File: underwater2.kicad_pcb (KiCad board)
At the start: 2 copper layers, 99.6 x 99.1 mm, 125 parts, among them IC1 KST10MTF, IC2 KST10MTF, IC3 ACT4070BYH-T, IC4 ICM-20948, IC5 MAX662ACSA+, IC6 MCP73842T-840I_UN, J1 Conn_01x10_Female, J10 momentary switch, J11 external regurator, J12 ICM20948 out, J13 Motor1, J14 MotorPow, J15 Motor2, J16 Conn_01x02_Female, J17 Conn_01x02_Female, J18 Conn_01x02_Female, J2 USB_C_Receptacle_USB2.0, J3 Raspberry_Pi_2_3, J4 serial, J5 Water, J6 serial2, J7 5v pow, J8 5v pow, J9 Power, Q1 2SC2712-Y,LF, Q2 2SC2712-Y,LF, Q3 2SC2712-Y,LF, Q4 2SC2712-Y,LF, Q5 2SC2712-Y,LF, Q6 2SC2712-Y,LF, Q7 2SC2712-Y,LF, Q8 2SC2712-Y,LF, Q9 NDS8434, SW1 SW_Push_Dual, SW2 SW_Push_Dual, SW3 SW_DIP_x01, U1 FT232RL, U2 LM1117-3.3, U3 TB6612FNG, U4 ESP32-WROOM-32, U5 LM1117-1.8, U6 TB6612FNG

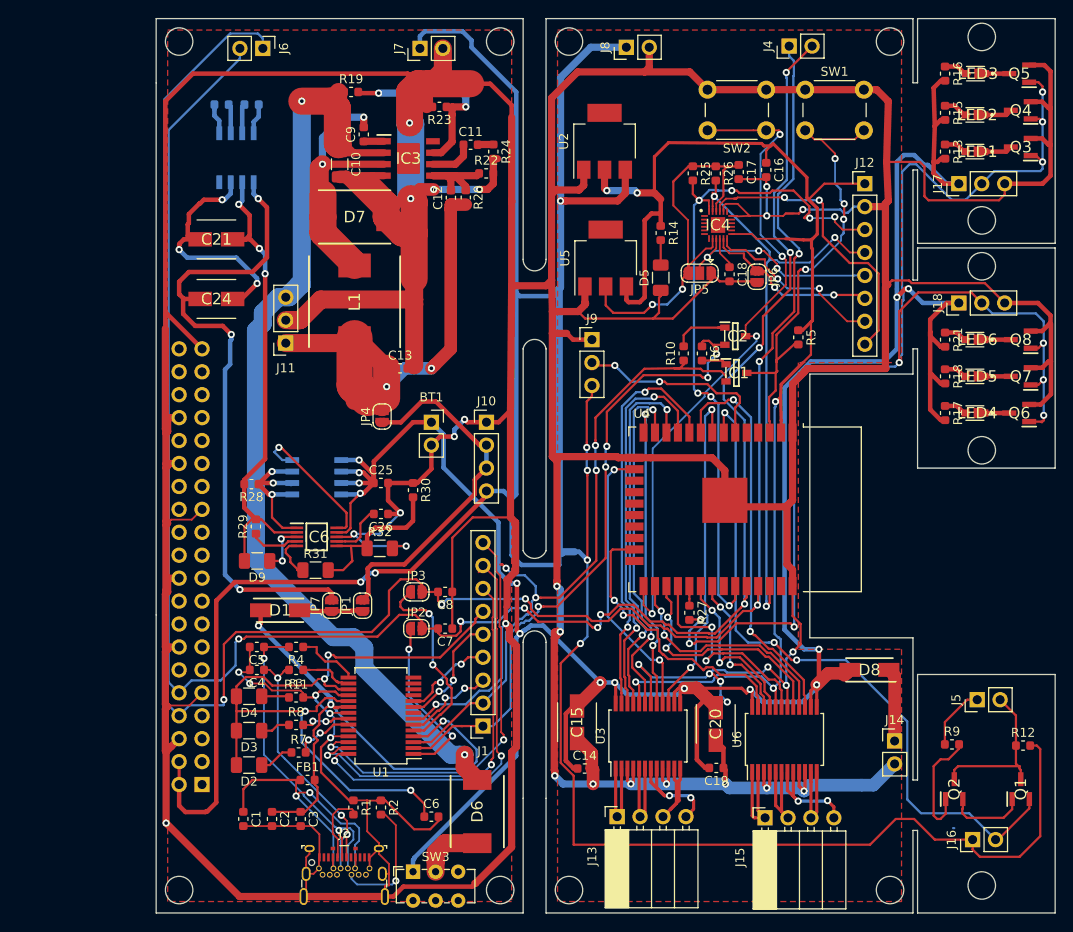
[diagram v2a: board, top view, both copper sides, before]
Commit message: Modified drive ESC and external switch.
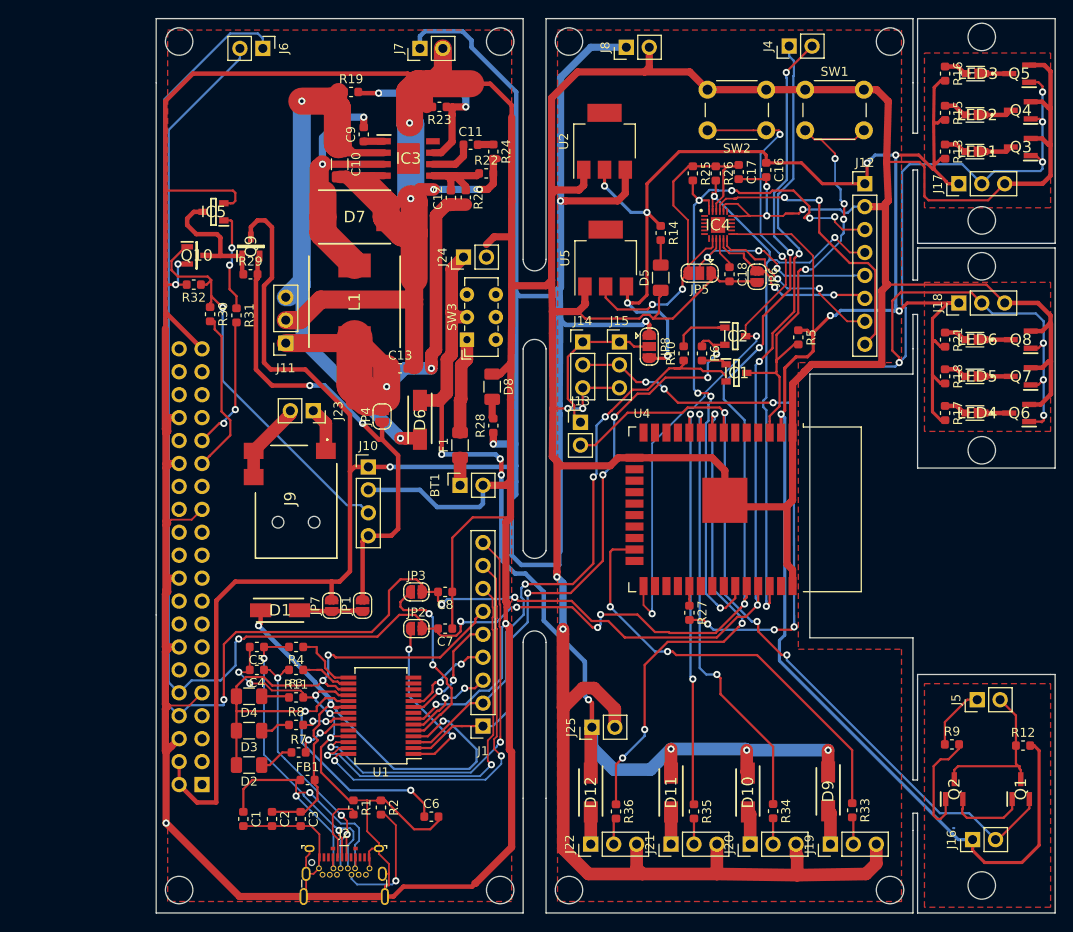
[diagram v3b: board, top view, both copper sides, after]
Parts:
- removed C14, C19, C26: 0.1μF, Capacitor_SMD:C_0603_1608Metric
- removed C15, C20, C21: 10μF, SamacSys_Parts:865080640004
- removed C22, C23: 0.22μF, Capacitor_SMD:C_0603_1608Metric
- removed C24: 4.7uF, SamacSys_Parts:865080640004
- removed C25: 10μF, Capacitor_SMD:C_0603_1608Metric
- removed IC6: MCP73842T-840I_UN, SamacSys_Parts:SOP50P490X110-10N
- removed U3, U6: TB6612FNG, Package_SO:SSOP-24_5.3x8.2mm_P0.65mm
- added D10: 34/40V 3A, SamacSys_Parts:DIOM5226X240N, F.Cu at (157.0, 126.4)
- added D11: 34/40V 3A, SamacSys_Parts:DIOM5226X240N, F.Cu at (148.5, 126.4)
- added D12: 34/40V 3A, SamacSys_Parts:DIOM5226X240N, F.Cu at (139.6, 126.4)
- added F1: fuse 10A, Resistor_SMD:R_1206_3216Metric, F.Cu at (125.1, 87.9)
- added J19: BLMOTOR_B2, Connector_PinHeader_2.54mm:PinHeader_1x03_P2.54mm_Vertical, F.Cu at (166.1, 132.1)
- added J20: BLMOTOR_B1, Connector_PinHeader_2.54mm:PinHeader_1x03_P2.54mm_Vertical, F.Cu at (157.2, 132.1)
- added J21: BLMOTOR_A2, Connector_PinHeader_2.54mm:PinHeader_1x03_P2.54mm_Vertical, F.Cu at (148.5, 132.1)
- added J22: BLMOTOR_A1, Connector_PinHeader_2.54mm:PinHeader_1x03_P2.54mm_Vertical, F.Cu at (139.6, 132.1)
- added J23: BATT Chrg, Connector_PinSocket_2.54mm:PinSocket_1x02_P2.54mm_Vertical, F.Cu at (108.8, 84.1)
- added J24: BT pow, Connector_PinHeader_2.54mm:PinHeader_1x02_P2.54mm_Vertical, F.Cu at (125.5, 67.1)
- added J25: BT pow, Connector_PinHeader_2.54mm:PinHeader_1x02_P2.54mm_Vertical, F.Cu at (139.7, 119.1)
- added JP8: SolderJumper_3_Open, Jumper:SolderJumper-3_P1.3mm_Open_RoundedPad1.0x1.5mm, F.Cu at (146.1, 77.0)
- added Q10: IRLML6344TRPBF, SOT95P237X112-3N, F.Cu at (95.9, 66.9)
- added R33: 100, Capacitor_SMD:C_0603_1608Metric, F.Cu at (168.5, 128.3)
- added R34: 100, Capacitor_SMD:C_0603_1608Metric, F.Cu at (159.8, 128.4)
- added R35: 100, Capacitor_SMD:C_0603_1608Metric, F.Cu at (151.0, 128.5)
- added R36: 100, Capacitor_SMD:C_0603_1608Metric, F.Cu at (142.4, 128.5)
- BT1: value Battery -> BATT in
- D4: value POWER -> Pwr USB
- D5: value Power 3.3 -> Pwr 3.3V
- D6: footprint SamacSys_Parts:DIONM7959X282N -> SamacSys_Parts:DIOM5226X240N
- D8: value DIODE -> Pwr 5V; footprint SamacSys_Parts:DIOM5226X240N -> Capacitor_SMD:C_1206_3216Metric
- D9: value LED_Small -> 34/40V 3A; footprint Capacitor_SMD:C_1206_3216Metric -> SamacSys_Parts:DIOM5226X240N
- IC1, IC2: footprint SamacSys_Parts:SOT95P240X120-3N -> SOT95P240X120-3N
- IC3: footprint SamacSys_Parts:SOIC127P600X170-9N -> SOIC127P600X170-9N
- IC5: value MAX662ACSA+ -> KST10MTF; footprint SamacSys_Parts:SOIC127P600X175-8N -> SOT95P240X120-3N; moved to F.Cu
- J1: value Conn_01x10_Female -> test con
- J11: value external regurator -> ext regurator
- J13: value Motor1 -> Water Sence; footprint Connector_PinSocket_2.54mm:PinSocket_1x04_P2.54mm_Horizontal -> Connector_PinHeader_2.54mm:PinHeader_1x02_P2.54mm_Vertical
- J14: value MotorPow -> LED Left; footprint Connector_PinHeader_2.54mm:PinHeader_1x02_P2.54mm_Vertical -> Connector_PinHeader_2.54mm:PinHeader_1x03_P2.54mm_Vertical
- J15: value Motor2 -> LED right; footprint Connector_PinSocket_2.54mm:PinSocket_1x04_P2.54mm_Horizontal -> Connector_PinHeader_2.54mm:PinHeader_1x03_P2.54mm_Vertical
- J16: value Conn_01x02_Female -> Water con
- J17: value Conn_01x02_Female -> LED left con
- J18: value Conn_01x02_Female -> LED right con
- J9: value Power -> PJ1-021-SMT-TR; footprint Connector_PinHeader_2.54mm:PinHeader_1x03_P2.54mm_Vertical -> PJ1021SMTTR
- JP4: value J battpower -> BATT power
- LED1, LED2, LED3, LED4, LED5, LED6: footprint SamacSys_Parts:MP201611006570 -> MP201611006570
- Q1, Q2, Q3, Q4, Q5, Q6, Q7, Q8: footprint SamacSys_Parts:SOT95P260X140-3N -> SOT95P260X140-3N
- Q9: value NDS8434 -> DMP3099L-7; footprint SamacSys_Parts:SOIC127P600X175-8N -> SOT96P240X120-3N; moved to F.Cu
- R28: value 100m -> 270
- R30: value R_Variable -> 39k
- R31: value sermal1 -> 1k; footprint Capacitor_SMD:C_1206_3216Metric -> Capacitor_SMD:C_0603_1608Metric
- R32: value sermal2 -> 100k; footprint Capacitor_SMD:C_1206_3216Metric -> Capacitor_SMD:C_0603_1608Metric
- moved D9 68.2 mm to (165.9, 126.2), turned to 270 degrees
- moved SW3 59.2 mm to (125.9, 76.2), turned to 90 degrees
- moved J14 56.1 mm to (138.7, 76.5)
- moved J15 55.1 mm to (142.7, 76.5), turned to 0 degrees
- moved D8 52.2 mm to (128.7, 81.4), turned to 270 degrees
- moved J13 43.9 mm to (138.4, 85.3), turned to 0 degrees
- moved D6 43.8 mm to (120.7, 85.1), turned to 270 degrees
- moved J9 37.4 mm to (106.9, 94.2), turned to 90 degrees
- moved R32 35.7 mm to (95.6, 70.1), turned to 180 degrees
- moved R30 29.7 mm to (97.4, 73.4)
- moved R31 29.5 mm to (100.3, 73.5), turned to 270 degrees
- moved R29 27.9 mm to (101.9, 69.0), turned to 0 degrees
- moved R28 27.6 mm to (128.8, 85.7), turned to 90 degrees
- moved Q9 26.6 mm to (101.9, 65.9), turned to 90 degrees
- moved J10 14.0 mm to (114.9, 90.3)
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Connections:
- BT1 pad 1: +BATT -> Net-(BT1-Pad1)
- D6 pad 1: Net-(D6-Pad1) -> +BATT
- D8 pad 1: Net-(D8-Pad1) -> -BATT
- D8 pad 2: +BATT -> Net-(D8-Pad2)
- D9 pad 1: Net-(D9-Pad1) -> +BATT
- D9 pad 2: Net-(C21-Pad1) -> Net-(D9-Pad2)
- IC5 pad 1: Net-(C22-Pad1) -> Net-(IC5-Pad1)
- IC5 pad 2: Net-(C22-Pad2) -> -BATT
- IC5 pad 3: Net-(C23-Pad1) -> Net-(IC5-Pad3)
- J10 pad 1: -BATT -> +5V
- J10 pad 2: +VSW -> -BATT
- J10 pad 3: +VSW -> Net-(J10-Pad3)
- J10 pad 4: +5V -> +VSW
- J13 pad 2: Net-(J13-Pad2) -> WATER
- J14 pad 1: Net-(D8-Pad1) -> Net-(J13-Pad1)
- J14 pad 2: -BATT -> LED_SW
- J15 pad 1: Net-(J15-Pad1) -> Net-(J13-Pad1)
- J15 pad 2: Net-(J15-Pad2) -> LED_SW
- J15 pad 3: Net-(J15-Pad3) -> -BATT
- J16 pad 1: +5V -> +3V3
- J17 pad 1: +BATT -> +3V3
- J18 pad 1: +BATT -> +3V3
- J3 pad 29: (no net) -> GPIO5
- J3 pad 31: (no net) -> GPIO6
- J9 pad 1: -BATT -> Net-(J23-Pad1)
- J9 pad 2: power -> -BATT
- J9 pad 3: +5V -> -BATT
- JP7 pad 2: VCC -> +5V
- Q9 pad 1: Net-(IC6-Pad1) -> Net-(IC5-Pad3)
- Q9 pad 2: Net-(IC6-Pad1) -> +VSW
- Q9 pad 3: Net-(IC6-Pad1) -> +5V
- R12 pad 2: +5V -> +3V3
- R13 pad 2: +BATT -> +3V3
- R15 pad 2: +BATT -> +3V3
- R16 pad 2: +BATT -> +3V3
- R17 pad 2: +BATT -> +3V3
- R18 pad 2: +BATT -> +3V3
- R21 pad 2: +BATT -> +3V3
- R28 pad 1: Net-(IC6-Pad1) -> +5V
- R28 pad 2: Net-(C21-Pad1) -> Net-(D8-Pad2)
- R29 pad 1: Net-(IC6-Pad4) -> Net-(IC5-Pad3)
- R29 pad 2: Net-(C21-Pad1) -> +VSW
- R30 pad 1: -BATT -> Net-(J10-Pad3)
- R30 pad 2: Net-(IC6-Pad6) -> GPIO5
- R31 pad 1: Net-(IC6-Pad5) -> Net-(IC5-Pad1)
- R31 pad 2: Net-(IC6-Pad6) -> GPIO6
- R32 pad 1: Net-(IC6-Pad6) -> Net-(J10-Pad3)
- SW3 pad 1: +BATT -> Net-(F1-Pad2)
- SW3 pad 2: Net-(D6-Pad1) -> +BATT
- U4 pad 11: IO26 -> (no net)
- U4 pad 12: IO27 -> (no net)
- U4 pad 13: IO14 -> (no net)
- U4 pad 14: IO12 -> (no net)
- U4 pad 16: IO13 -> (no net)
- U4 pad 26: IO4 -> (no net)
- U4 pad 27: IO16 -> (no net)
- U4 pad 28: IO17 -> (no net)
- U4 pad 30: IO18 -> (no net)
- U4 pad 31: IO19 -> (no net)
- U4 pad 6: power -> (no net)
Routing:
- net +BATT: track 302.1 -> 111.7 mm, vias 14 -> 7
- net +3V3: track 159.1 -> 260.8 mm, vias 5 -> 9
- net VCC: track 72.0 -> 0.00 mm, vias 3 -> 0
- net +5V: track 345.4 -> 281.5 mm, vias 7 -> 4
- net -BATT: track 1037.0 -> 979.1 mm, vias 39 -> 21
- net Net-(C21-Pad1): track 54.3 -> 0.00 mm, vias 3 -> 0
- net Net-(J10-Pad3): track 0.00 -> 44.8 mm, vias 0 -> 1
- net Net-(C10-Pad1): track 111.3 -> 67.0 mm
- net IO26: track 43.2 -> 0.00 mm, vias 2 -> 0
- net IO27: track 41.6 -> 0.00 mm, vias 2 -> 0
- net IO14: track 39.7 -> 0.00 mm, vias 2 -> 0
- net IO12: track 35.1 -> 0.00 mm, vias 2 -> 0
- net IO13: track 31.5 -> 0.00 mm, vias 2 -> 0
- net IO16: track 26.6 -> 0.00 mm, vias 2 -> 0
- net IO4: track 26.3 -> 0.00 mm, vias 2 -> 0
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- added copper zone on F.Cu, net (none)
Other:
- outline, holes or cut-outs redrawn
